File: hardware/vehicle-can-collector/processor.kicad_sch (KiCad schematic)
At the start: 11 parts, among them SW201 SW_Push, U201 ATSAMC21J18A-AUT, U202 PL133-37TI, U203 ADM6320BX33ARJZ-R7, X201 ASV-12.000MHZ-EJ-T, Y201 32.768kHz

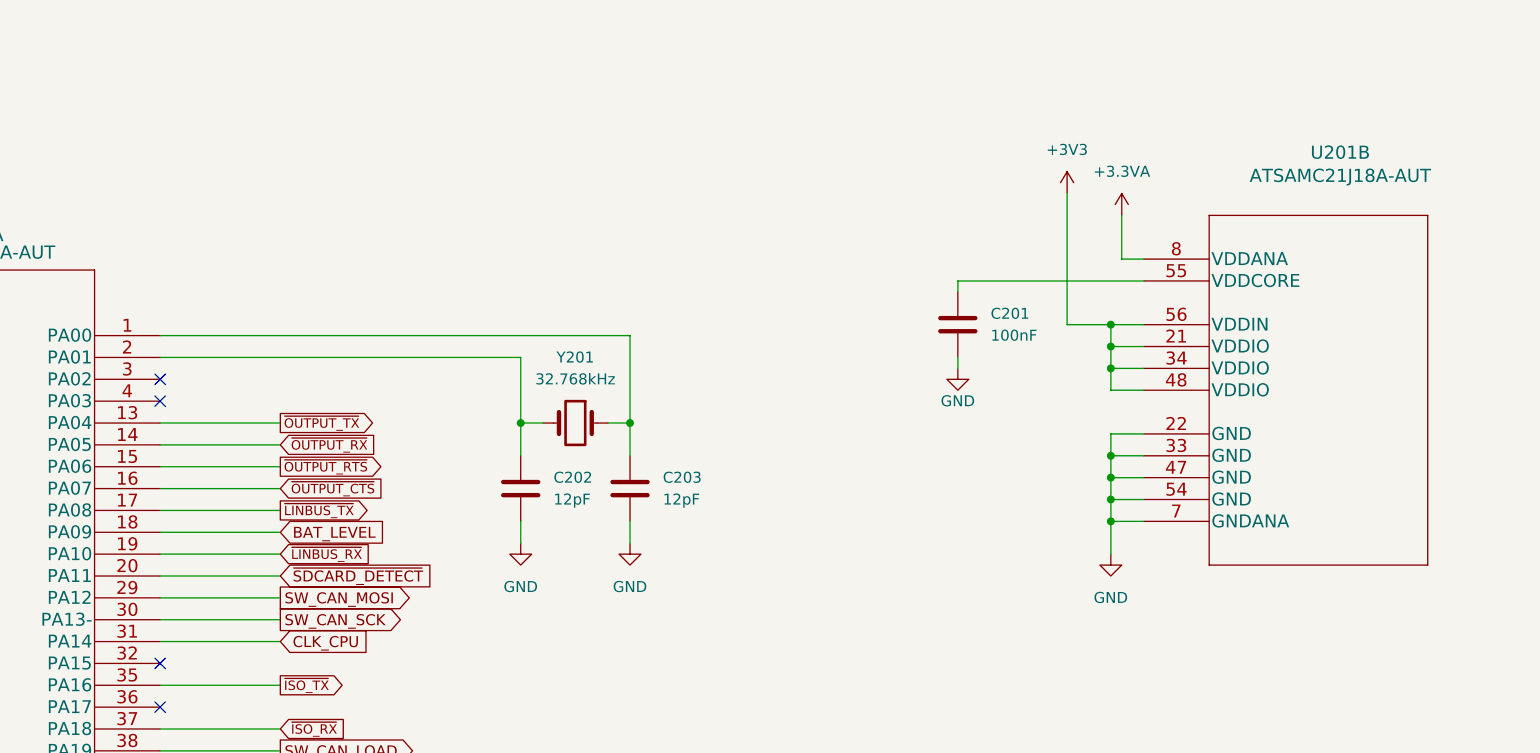
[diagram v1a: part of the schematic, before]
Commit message: Added footprints, tossed all footprints onto PCB
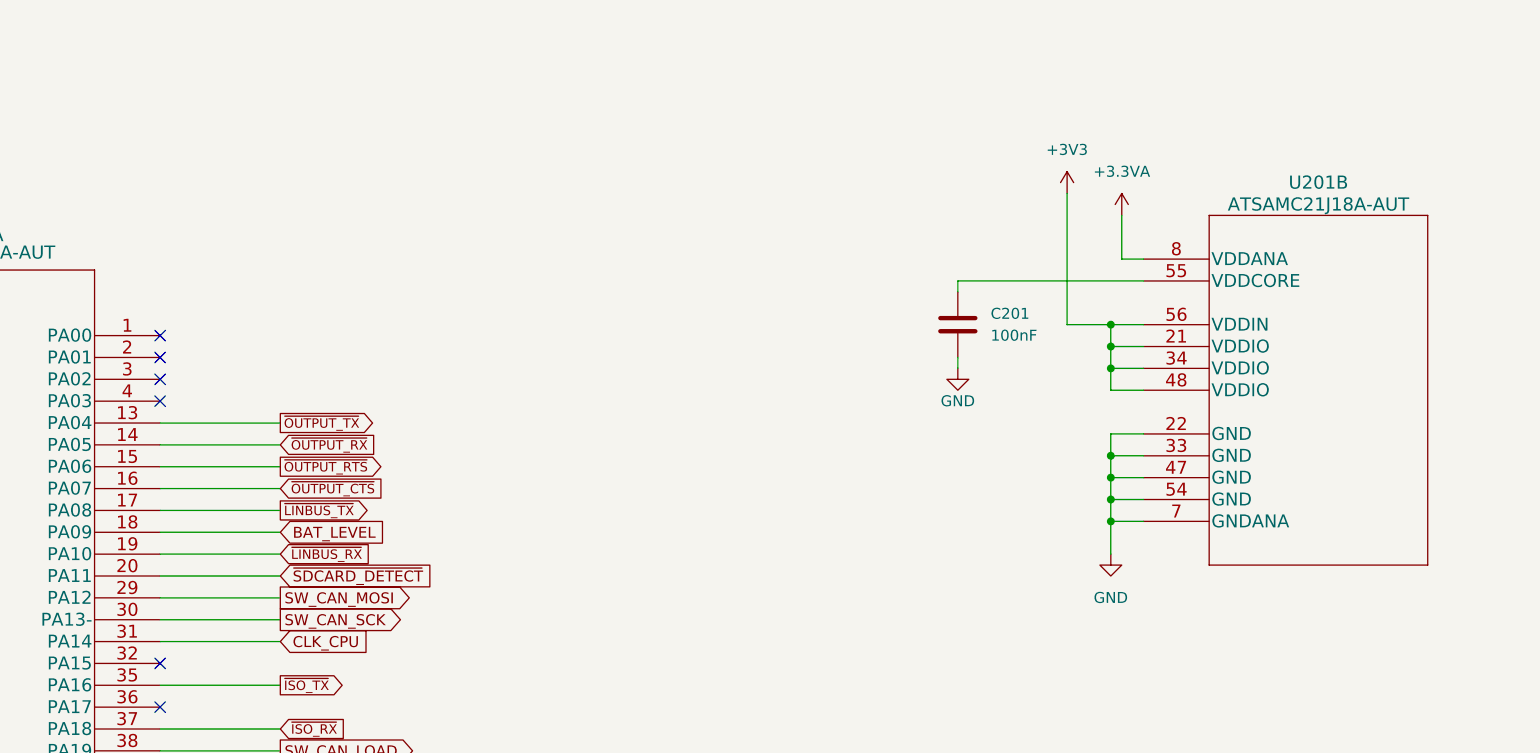
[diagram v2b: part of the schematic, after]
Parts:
- removed C202, C203: 12pF, symbol Device:C
- removed Y201: 32.768kHz, Crystal:Crystal_HC18-U_Horizontal, symbol Device:Crystal
- C201: footprint (none) -> Capacitor_SMD:C_0805_2012Metric_Pad1.18x1.45mm_HandSolder
- R201, R202: footprint (none) -> Resistor_SMD:R_0805_2012Metric_Pad1.20x1.40mm_HandSolder
- SW201: footprint (none) -> Button_Switch_THT:SW_PUSH_6mm
- U201: footprint TQFP64_10x10MC_MCH -> UltraLibrarian:ATSAMC21J18A-AUT
- U202: footprint SOT-23-6_MC_MCH -> UltraLibrarian:PL133-37TI
- U203: footprint RJ_5_ADI -> UltraLibrarian:ADM6320BX33ARJZ-R7
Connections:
- no-connect marks 12 -> 14
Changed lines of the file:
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@@
   (junction (at 234.95 69.85) (diameter 0) (color 0 0 0 0)
   )
-  (junction (at 179.07 66.04) (diameter 0) (color 0 0 0 0)
-  )
   (junction (at 107.95 165.1) (diameter 0) (color 0 0 0 0)
   )
@@
   )
   (junction (at 107.95 147.32) (diameter 0) (color 0 0 0 0)
-  )
-  (junction (at 166.37 66.04) (diameter 0) (color 0 0 0 0)
   )
   (junction (at 234.95 77.47) (diameter 0) (color 0 0 0 0)
@@
   (no_connect (at 78.74 55.88))
   (no_connect (at 78.74 60.96))
+  (no_connect (at 124.46 58.42))
   (no_connect (at 78.74 76.2))
   (no_connect (at 124.46 93.98))
   (no_connect (at 78.74 68.58))
+  (no_connect (at 124.46 55.88))
   (no_connect (at 124.46 63.5))
   (no_connect (at 123.19 167.64))
@@
     (stroke (width 0) (type default) (color 0 0 0 0))
   )
-  (wire (pts (xy 124.46 55.88) (xy 179.07 55.88))
-    (stroke (width 0) (type default) (color 0 0 0 0))
-  )
-  (wire (pts (xy 124.46 58.42) (xy 166.37 58.42))
-    (stroke (width 0) (type default) (color 0 0 0 0))
-  )
   (wire (pts (xy 217.17 49.53) (xy 238.76 49.53))
     (stroke (width 0) (type default) (color 0 0 0 0))
@@
     (stroke (width 0) (type default) (color 0 0 0 0))
   )
-  (wire (pts (xy 166.37 66.04) (xy 166.37 69.85))
-    (stroke (width 0) (type default) (color 0 0 0 0))
-  )
   (wire (pts (xy 124.46 121.92) (xy 138.43 121.92))
     (stroke (width 0) (type default) (color 0 0 0 0))
@@
     (stroke (width 0) (type default) (color 0 0 0 0))
   )
-  (wire (pts (xy 179.07 69.85) (xy 179.07 66.04))
-    (stroke (width 0) (type default) (color 0 0 0 0))
-  )
   (wire (pts (xy 123.19 165.1) (xy 107.95 165.1))
     (stroke (width 0) (type default) (color 0 0 0 0))
@@
     (stroke (width 0) (type default) (color 0 0 0 0))
   )
-  (wire (pts (xy 166.37 58.42) (xy 166.37 66.04))
-    (stroke (width 0) (type default) (color 0 0 0 0))
-  )
   (wire (pts (xy 234.95 57.15) (xy 238.76 57.15))
     (stroke (width 0) (type default) (color 0 0 0 0))
@@
     (stroke (width 0) (type default) (color 0 0 0 0))
   )
-  (wire (pts (xy 166.37 66.04) (xy 168.91 66.04))
-    (stroke (width 0) (type default) (color 0 0 0 0))
-  )
   (wire (pts (xy 67.31 71.12) (xy 78.74 71.12))
     (stroke (width 0) (type default) (color 0 0 0 0))
@@
     (stroke (width 0) (type default) (color 0 0 0 0))
   )
-  (wire (pts (xy 176.53 66.04) (xy 179.07 66.04))
-    (stroke (width 0) (type default) (color 0 0 0 0))
-  )
   (wire (pts (xy 124.46 71.12) (xy 138.43 71.12))
     (stroke (width 0) (type default) (color 0 0 0 0))
@@
     (stroke (width 0) (type default) (color 0 0 0 0))
   )
-  (wire (pts (xy 179.07 77.47) (xy 179.07 80.01))
-    (stroke (width 0) (type default) (color 0 0 0 0))
-  )
   (wire (pts (xy 67.31 99.06) (xy 78.74 99.06))
     (stroke (width 0) (type default) (color 0 0 0 0))
   )
-  (wire (pts (xy 166.37 77.47) (xy 166.37 80.01))
-    (stroke (width 0) (type default) (color 0 0 0 0))
-  )
   (wire (pts (xy 201.93 129.54) (xy 201.93 127))
     (stroke (width 0) (type default) (color 0 0 0 0))
   )
   (wire (pts (xy 67.31 88.9) (xy 78.74 88.9))
-    (stroke (width 0) (type default) (color 0 0 0 0))
-  )
-  (wire (pts (xy 179.07 66.04) (xy 179.07 55.88))
     (stroke (width 0) (type default) (color 0 0 0 0))
   )
@@
       (effects (font (size 1.27 1.27)) (justify left))
     )
-    (property "Footprint" "" (id 2) (at 96.012 154.94 90)
+    (property "Footprint" "Resistor_SMD:R_0805_2012Metric_Pad1.20x1.40mm_HandSolder" (id 2) (at 96.012 154.94 90)
       (effects (font (size 1.27 1.27)) hide)
     )
@@
     )
     (pin "1")
-  )
-  (symbol (lib_id "Device:C") (at 179.07 73.66 0) (unit 1)
-    (in_bom yes) (on_board yes) (fields_autoplaced)
-    (property "Reference" "C203" (id 0) (at 182.88 72.3899 0)
-      (effects (font (size 1.27 1.27)) (justify left))
-    )
-    (property "Value" "12pF" (id 1) (at 182.88 74.9299 0)
-      (effects (font (size 1.27 1.27)) (justify left))
-    )
-    (property "Footprint" "" (id 2) (at 180.0352 77.47 0)
-      (effects (font (size 1.27 1.27)) hide)
-    )
-    (property "Datasheet" "~" (id 3) (at 179.07 73.66 0)
-      (effects (font (size 1.27 1.27)) hide)
-    )
-    (pin "1")
-    (pin "2")
   )
   (symbol (lib_id "power:+3V3") (at 116.84 146.05 0) (unit 1)
@@
       (effects (font (size 1.524 1.524)) (justify left))
     )
-    (property "Footprint" "TQFP64_10x10MC_MCH" (id 2) (at 101.6 47.244 0)
+    (property "Footprint" "UltraLibrarian:ATSAMC21J18A-AUT" (id 2) (at 101.6 47.244 0)
       (effects (font (size 1.524 1.524)) hide)
     )
-    (property "Datasheet" "https://www.st.com/resource/en/datasheet/lm139.pdf" (id 3) (at 78.74 55.88 0)
+    (property "Datasheet" "" (id 3) (at 78.74 55.88 0)
       (effects (font (size 1.524 1.524)) hide)
     )
@@
     (pin "9")
   )
-  (symbol (lib_id "Device:Crystal") (at 172.72 66.04 0) (mirror y) (unit 1)
-    (in_bom yes) (on_board yes) (fields_autoplaced)
-    (property "Reference" "Y201" (id 0) (at 172.72 58.42 0))
-    (property "Value" "32.768kHz" (id 1) (at 172.72 60.96 0))
-    (property "Footprint" "Crystal:Crystal_HC18-U_Horizontal" (id 2) (at 172.72 66.04 0)
-      (effects (font (size 1.27 1.27)) hide)
-    )
-    (property "Datasheet" "~" (id 3) (at 172.72 66.04 0)
-      (effects (font (size 1.27 1.27)) hide)
-    )
-    (pin "1")
-    (pin "2")
-  )
   (symbol (lib_id "UltraLibrarian:ATSAMC21J18A-AUT") (at 238.76 46.99 0) (unit 2)
     (in_bom yes) (on_board yes)
-    (property "Reference" "U201" (id 0) (at 261.62 34.6202 0)
+    (property "Reference" "U201" (id 0) (at 259.08 38.1 0)
       (effects (font (size 1.524 1.524)))
     )
-    (property "Value" "ATSAMC21J18A-AUT" (id 1) (at 261.62 37.3126 0)
+    (property "Value" "ATSAMC21J18A-AUT" (id 1) (at 259.08 40.64 0)
       (effects (font (size 1.524 1.524)))
     )
-    (property "Footprint" "TQFP64_10x10MC_MCH" (id 2) (at 261.62 38.354 0)
+    (property "Footprint" "UltraLibrarian:ATSAMC21J18A-AUT" (id 2) (at 261.62 38.354 0)
       (effects (font (size 1.524 1.524)) hide)
     )
-    (property "Datasheet" "https://www.st.com/resource/en/datasheet/lm139.pdf" (id 3) (at 238.76 46.99 0)
+    (property "Datasheet" "" (id 3) (at 238.76 46.99 0)
       (effects (font (size 1.524 1.524)) hide)
     )
@@
       (effects (font (size 1.524 1.524)))
     )
-    (property "Footprint" "SOT-23-6_MC_MCH" (id 2) (at 245.11 132.334 0)
+    (property "Footprint" "UltraLibrarian:PL133-37TI" (id 2) (at 245.11 132.334 0)
       (effects (font (size 1.524 1.524)) hide)
     )
@@
     (pin "1")
   )
-  (symbol (lib_id "power:GND") (at 179.07 80.01 0) (unit 1)
-    (in_bom yes) (on_board yes) (fields_autoplaced)
-    (property "Reference" "#PWR0205" (id 0) (at 179.07 86.36 0)
-      (effects (font (size 1.27 1.27)) hide)
-    )
-    (property "Value" "GND" (id 1) (at 179.07 85.09 0))
-    (property "Footprint" "" (id 2) (at 179.07 80.01 0)
-      (effects (font (size 1.27 1.27)) hide)
-    )
-    (property "Datasheet" "" (id 3) (at 179.07 80.01 0)
-      (effects (font (size 1.27 1.27)) hide)
-    )
-    (pin "1")
-  )
   (symbol (lib_id "Device:C") (at 217.17 54.61 0) (unit 1)
     (in_bom yes) (on_board yes) (fields_autoplaced)
@@
       (effects (font (size 1.27 1.27)) (justify left))
     )
-    (property "Footprint" "" (id 2) (at 218.1352 58.42 0)
+    (property "Footprint" "Capacitor_SMD:C_0805_2012Metric_Pad1.18x1.45mm_HandSolder" (id 2) (at 218.1352 58.42 0)
       (effects (font (size 1.27 1.27)) hide)
     )
@@
     (pin "1")
   )
-  (symbol (lib_id "Device:C") (at 166.37 73.66 0) (unit 1)
-    (in_bom yes) (on_board yes) (fields_autoplaced)
-    (property "Reference" "C202" (id 0) (at 170.18 72.3899 0)
-      (effects (font (size 1.27 1.27)) (justify left))
-    )
-    (property "Value" "12pF" (id 1) (at 170.18 74.9299 0)
-      (effects (font (size 1.27 1.27)) (justify left))
-    )
-    (property "Footprint" "" (id 2) (at 167.3352 77.47 0)
-      (effects (font (size 1.27 1.27)) hide)
-    )
-    (property "Datasheet" "~" (id 3) (at 166.37 73.66 0)
-      (effects (font (size 1.27 1.27)) hide)
-    )
-    (pin "1")
-    (pin "2")
-  )
-  (symbol (lib_id "power:GND") (at 166.37 80.01 0) (unit 1)
-    (in_bom yes) (on_board yes) (fields_autoplaced)
-    (property "Reference" "#PWR0204" (id 0) (at 166.37 86.36 0)
-      (effects (font (size 1.27 1.27)) hide)
-    )
-    (property "Value" "GND" (id 1) (at 166.37 85.09 0))
-    (property "Footprint" "" (id 2) (at 166.37 80.01 0)
-      (effects (font (size 1.27 1.27)) hide)
-    )
-    (property "Datasheet" "" (id 3) (at 166.37 80.01 0)
-      (effects (font (size 1.27 1.27)) hide)
-    )
-    (pin "1")
-  )
   (symbol (lib_id "power:+3V3") (at 220.98 132.08 0) (unit 1)
     (in_bom yes) (on_board yes) (fields_autoplaced)
@@
       (effects (font (size 1.27 1.27)) (justify left))
     )
-    (property "Footprint" "" (id 2) (at 106.172 154.94 90)
+    (property "Footprint" "Resistor_SMD:R_0805_2012Metric_Pad1.20x1.40mm_HandSolder" (id 2) (at 106.172 154.94 90)
       (effects (font (size 1.27 1.27)) hide)
     )
@@
       (effects (font (size 1.524 1.524)) (justify left))
     )
-    (property "Footprint" "RJ_5_ADI" (id 2) (at 143.51 153.924 0)
+    (property "Footprint" "UltraLibrarian:ADM6320BX33ARJZ-R7" (id 2) (at 143.51 153.924 0)
       (effects (font (size 1.524 1.524)) hide)
     )
@@
     (property "Reference" "SW201" (id 0) (at 87.63 154.94 0))
     (property "Value" "SW_Push" (id 1) (at 87.63 157.48 0))
-    (property "Footprint" "" (id 2) (at 87.63 157.48 0)
-      (effects (font (size 1.27 1.27)) hide)
-    )
+    (property "Footprint" "Button_Switch_THT:SW_PUSH_6mm" (id 2) (at 87.63 157.48 0)
+      (effects (font (size 1.27 1.27)) hide)
+    )
